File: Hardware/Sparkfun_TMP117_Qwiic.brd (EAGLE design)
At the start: 25.4 x 25.4 mm, 53 parts, among them J1 PTH, J2 QWIIC_RA, J3 QWIIC_RA, U1 TMP117

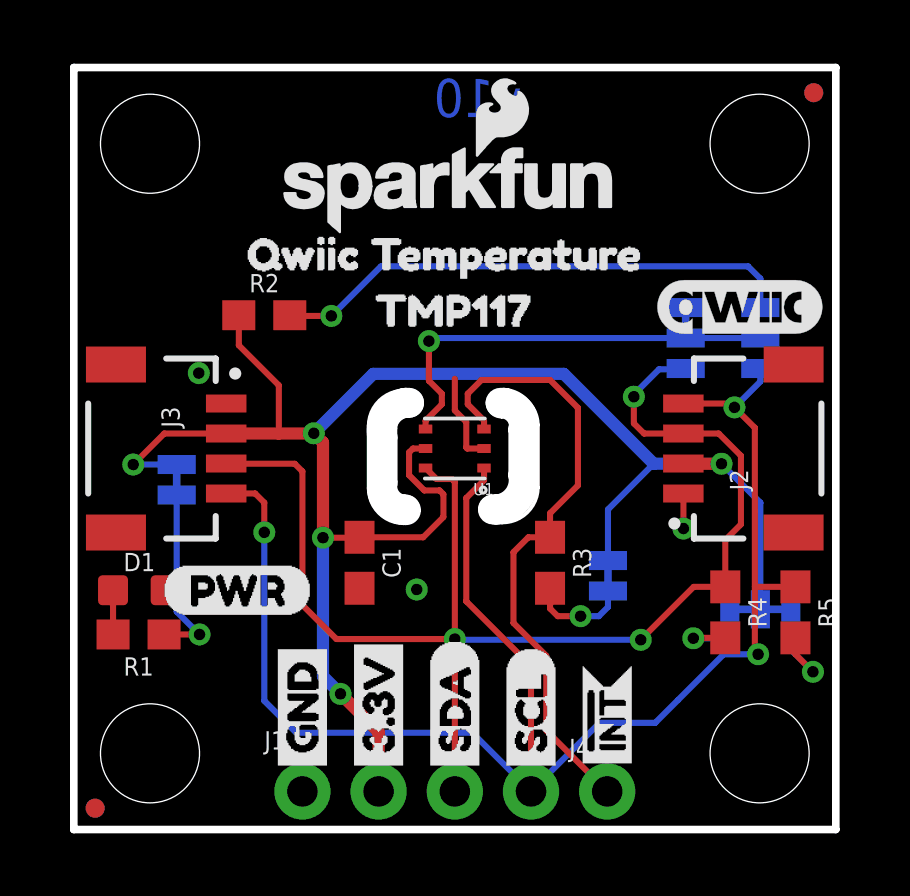
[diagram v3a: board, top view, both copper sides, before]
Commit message: 1st run of checklist
-version font type in schematic
-silk width bumped up to 8 mils on a couple jumpers and the tmp117 package
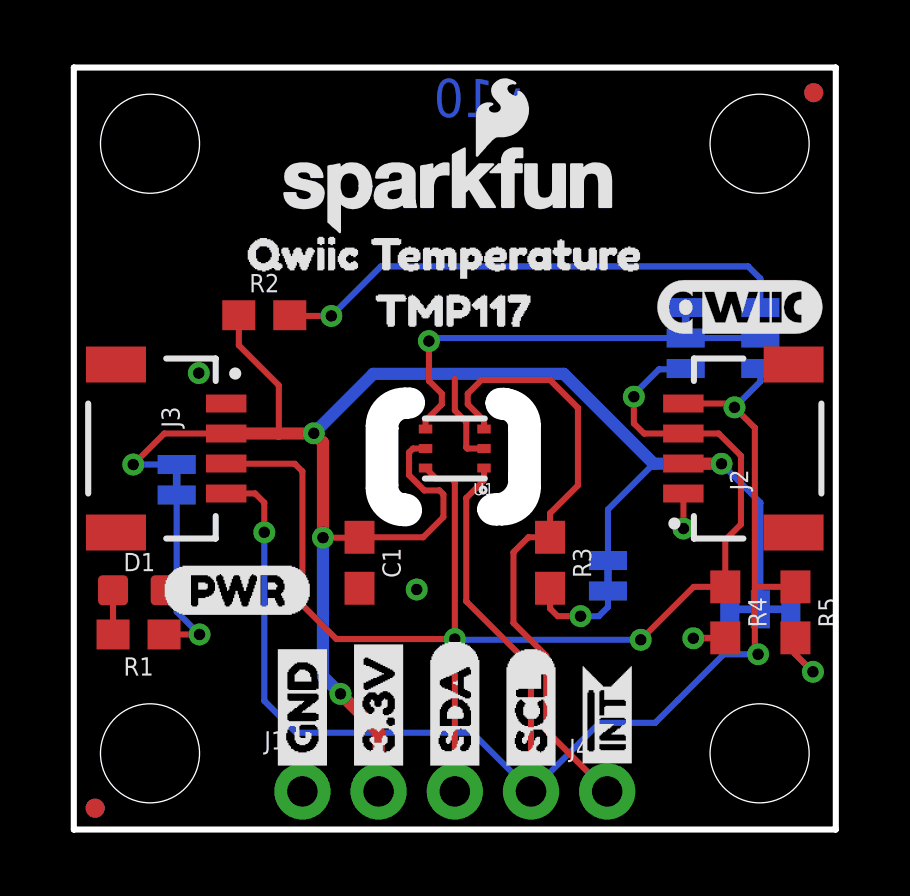
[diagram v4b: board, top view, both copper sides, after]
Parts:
- I2C: value (none) -> JUMPER-SMT_3_2-NC_TRACE_SILK
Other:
- outline, holes or cut-outs redrawn
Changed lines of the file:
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@@
 <setting verticaltext="up"/>
 </settings>
-<grid distance="0.05" unitdist="inch" unit="inch" style="lines" multiple="1" display="yes" altdistance="0.001" altunitdist="inch" altunit="inch"/>
+<grid distance="0.05" unitdist="inch" unit="inch" style="lines" multiple="1" display="yes" altdistance="0.0001" altunitdist="inch" altunit="inch"/>
 <layers>
 <layer number="1" name="Top" color="4" fill="1" visible="yes" active="yes"/>
@@
 <board>
 <plain>
-<wire x1="0" y1="0" x2="0" y2="25.4" width="0.254" layer="20"/>
-<wire x1="25.4" y1="0" x2="0" y2="0" width="0.254" layer="20"/>
-<wire x1="25.4" y1="25.4" x2="25.4" y2="0" width="0.254" layer="20"/>
-<wire x1="0" y1="25.4" x2="25.4" y2="25.4" width="0.254" layer="20"/>
+<wire x1="0" y1="0" x2="0" y2="25.4" width="0.2032" layer="20"/>
+<wire x1="25.4" y1="0" x2="0" y2="0" width="0.2032" layer="20"/>
+<wire x1="25.4" y1="25.4" x2="25.4" y2="0" width="0.2032" layer="20"/>
+<wire x1="0" y1="25.4" x2="25.4" y2="25.4" width="0.2032" layer="20"/>
 <text x="19.431" y="-7.366" size="1.778" layer="51" font="vector" ratio="12" align="top-left">Madison Chodikov,
 Pete Lewis</text>
@@
 <wire x1="11.049" y1="14.224" x2="11.176" y2="14.224" width="1" layer="46"/>
 <wire x1="10.922" y1="10.668" x2="11.049" y2="10.668" width="1" layer="46"/>
-<wire x1="10.7188" y1="13.3604" x2="10.7188" y2="11.4808" width="0.127" layer="20"/>
-<wire x1="10.7188" y1="11.4808" x2="11.0236" y2="11.0998" width="0.127" layer="20" curve="90"/>
-<wire x1="11.0236" y1="11.0998" x2="11.049" y2="11.0998" width="0.127" layer="20"/>
-<wire x1="11.049" y1="11.0998" x2="11.5062" y2="10.6426" width="0.127" layer="20" curve="-90"/>
-<wire x1="11.5062" y1="10.6426" x2="11.0744" y2="10.2108" width="0.127" layer="20" curve="-90"/>
-<wire x1="11.0744" y1="10.2108" x2="10.9982" y2="10.2108" width="0.127" layer="20"/>
-<wire x1="10.9982" y1="10.2108" x2="9.8298" y2="11.3792" width="0.127" layer="20" curve="-90"/>
-<wire x1="9.8298" y1="11.3792" x2="9.8298" y2="13.462" width="0.127" layer="20"/>
-<wire x1="9.8298" y1="13.462" x2="11.0236" y2="14.6304" width="0.127" layer="20" curve="-90"/>
-<wire x1="11.0236" y1="14.6304" x2="11.2014" y2="14.6304" width="0.127" layer="20"/>
-<wire x1="11.2014" y1="14.6304" x2="11.6078" y2="14.224" width="0.127" layer="20" curve="-90"/>
-<wire x1="11.6078" y1="14.224" x2="11.176" y2="13.7922" width="0.127" layer="20" curve="-90"/>
-<wire x1="11.176" y1="13.7922" x2="11.1252" y2="13.7922" width="0.127" layer="20"/>
-<wire x1="11.1252" y1="13.7922" x2="10.7188" y2="13.3858" width="0.127" layer="20" curve="90"/>
-<wire x1="10.7188" y1="13.3858" x2="10.7188" y2="13.3604" width="0.127" layer="20" curve="90"/>
-<wire x1="14.5796" y1="11.684" x2="14.5796" y2="13.3858" width="0.127" layer="20"/>
-<wire x1="14.5796" y1="13.3858" x2="14.2748" y2="13.7668" width="0.127" layer="20" curve="90"/>
-<wire x1="14.2748" y1="13.7668" x2="14.2494" y2="13.7668" width="0.127" layer="20"/>
-<wire x1="14.2494" y1="13.7668" x2="13.7922" y2="14.224" width="0.127" layer="20" curve="-90"/>
-<wire x1="13.7922" y1="14.224" x2="14.224" y2="14.605" width="0.127" layer="20" curve="-90"/>
-<wire x1="14.224" y1="14.605" x2="14.3002" y2="14.605" width="0.127" layer="20"/>
-<wire x1="14.3002" y1="14.605" x2="15.4686" y2="13.4874" width="0.127" layer="20" curve="-90"/>
-<wire x1="15.4686" y1="13.4874" x2="15.4686" y2="11.4046" width="0.127" layer="20"/>
-<wire x1="15.4686" y1="11.4046" x2="14.2748" y2="10.2362" width="0.127" layer="20" curve="-90"/>
-<wire x1="14.2748" y1="10.2362" x2="14.097" y2="10.2362" width="0.127" layer="20"/>
-<wire x1="14.097" y1="10.2362" x2="13.5382" y2="10.668" width="0.127" layer="20" curve="-90"/>
-<wire x1="13.5382" y1="10.668" x2="14.0208" y2="11.0998" width="0.127" layer="20" curve="-90"/>
-<wire x1="14.0208" y1="11.0998" x2="14.097" y2="11.0998" width="0.127" layer="20"/>
-<wire x1="14.097" y1="11.0998" x2="14.5796" y2="11.684" width="0.127" layer="20" curve="90"/>
+<wire x1="10.7188" y1="13.3604" x2="10.7188" y2="11.4808" width="0.2032" layer="20"/>
+<wire x1="10.7188" y1="11.4808" x2="11.0236" y2="11.0998" width="0.2032" layer="20" curve="90"/>
+<wire x1="11.0236" y1="11.0998" x2="11.049" y2="11.0998" width="0.2032" layer="20"/>
+<wire x1="11.049" y1="11.0998" x2="11.5062" y2="10.6426" width="0.2032" layer="20" curve="-90"/>
+<wire x1="11.5062" y1="10.6426" x2="11.0744" y2="10.2108" width="0.2032" layer="20" curve="-90"/>
+<wire x1="11.0744" y1="10.2108" x2="10.9982" y2="10.2108" width="0.2032" layer="20"/>
+<wire x1="10.9982" y1="10.2108" x2="9.8298" y2="11.3792" width="0.2032" layer="20" curve="-90"/>
+<wire x1="9.8298" y1="11.3792" x2="9.8298" y2="13.462" width="0.2032" layer="20"/>
+<wire x1="9.8298" y1="13.462" x2="11.0236" y2="14.6304" width="0.2032" layer="20" curve="-90"/>
+<wire x1="11.0236" y1="14.6304" x2="11.2014" y2="14.6304" width="0.2032" layer="20"/>
+<wire x1="11.2014" y1="14.6304" x2="11.6078" y2="14.224" width="0.2032" layer="20" curve="-90"/>
+<wire x1="11.6078" y1="14.224" x2="11.14551875" y2="13.79981875" width="0.2032" layer="20" curve="-90"/>
+<wire x1="11.14551875" y1="13.79981875" x2="11.09471875" y2="13.79981875" width="0.2032" layer="20"/>
+<wire x1="11.09471875" y1="13.79981875" x2="10.7188" y2="13.3858" width="0.2032" layer="20" curve="90"/>
+<wire x1="10.7188" y1="13.3858" x2="10.7188" y2="13.3604" width="0.2032" layer="20" curve="90"/>
+<wire x1="14.5796" y1="11.684" x2="14.5796" y2="13.3858" width="0.2032" layer="20"/>
+<wire x1="14.5796" y1="13.3858" x2="14.2748" y2="13.7668" width="0.2032" layer="20" curve="90"/>
+<wire x1="14.2748" y1="13.7668" x2="14.297659375" y2="13.75918125" width="0.2032" layer="20"/>
+<wire x1="14.297659375" y1="13.75918125" x2="13.822678125" y2="14.218921875" width="0.2032" layer="20" curve="-90"/>
+<wire x1="13.822678125" y1="14.218921875" x2="14.224" y2="14.599921875" width="0.2032" layer="20" curve="-90"/>
+<wire x1="14.224" y1="14.599921875" x2="14.3002" y2="14.605" width="0.2032" layer="20"/>
+<wire x1="14.3002" y1="14.605" x2="15.4686" y2="13.4874" width="0.2032" layer="20" curve="-90"/>
+<wire x1="15.4686" y1="13.4874" x2="15.4686" y2="11.4046" width="0.2032" layer="20"/>
+<wire x1="15.4686" y1="11.4046" x2="14.2748" y2="10.2362" width="0.2032" layer="20" curve="-90"/>
+<wire x1="14.2748" y1="10.2362" x2="14.097" y2="10.2362" width="0.2032" layer="20"/>
+<wire x1="14.097" y1="10.2362" x2="13.5382" y2="10.668" width="0.2032" layer="20" curve="-90"/>
+<wire x1="13.5382" y1="10.668" x2="14.0208" y2="11.0998" width="0.2032" layer="20" curve="-90"/>
+<wire x1="14.0208" y1="11.0998" x2="14.097" y2="11.0998" width="0.2032" layer="20"/>
+<wire x1="14.097" y1="11.0998" x2="14.5796" y2="11.684" width="0.2032" layer="20" curve="90"/>
 <text x="10.4902" y="11.049" size="0.3048" layer="20" rot="R90">ROUTE OUT</text>
 <text x="15.1384" y="11.1506" size="0.3048" layer="20" rot="R90">ROUTE OUT</text>
@@
 <element name="U$4" library="buzzard_labels" package="TMP1171" value="" x="9.144" y="17.2974" smashed="yes"/>
 <element name="U$6" library="buzzard_labels (2)" package="QWIIC_TEMPERATURE2" value="" x="4.8768" y="19.177" smashed="yes"/>
-<element name="I2C" library="SparkFun-Jumpers" library_urn="urn:adsk.eagle:library:528" package="SMT-JUMPER_3_2-NC_TRACE_SILK" package3d_urn="urn:adsk.eagle:package:39289/1" value="" x="22.8854" y="7.3406" smashed="yes" rot="MR0">
+<element name="I2C" library="SparkFun-Jumpers" package="SMT-JUMPER_3_2-NC_TRACE_SILK" package3d_urn="urn:adsk.eagle:package:39289/1" value="JUMPER-SMT_3_2-NC_TRACE_SILK" x="22.8854" y="7.3406" smashed="yes" rot="MR0">
 <attribute name="NAME" x="22.8854" y="8.4836" size="0.6096" layer="26" font="vector" ratio="20" rot="MR0" align="bottom-center"/>
 <attribute name="VALUE" x="22.8854" y="6.1976" size="0.6096" layer="28" font="vector" ratio="20" rot="MR0" align="top-center"/>
 </element>
-<element name="JP10" library="SparkFun-Jumpers" package="SMT-JUMPER_2_NC_TRACE_SILK" value="INT" x="17.8054" y="8.4582" smashed="yes" rot="MR90">
+<element name="JP10" library="SparkFun-Jumpers" package="SMT-JUMPER_2_NC_TRACE_SILK" package3d_urn="urn:adsk.eagle:package:39281/1" value="INT" x="17.8054" y="8.4582" smashed="yes" rot="MR90">
 <attribute name="NAME" x="19.0754" y="7.5057" size="0.4064" layer="26" rot="MR90"/>
 <attribute name="VALUE" x="16.1544" y="7.5057" size="0.4064" layer="28" rot="MR90"/>
@@
 <attribute name="VALUE" x="24.0284" y="16.383" size="0.6096" layer="28" font="vector" ratio="20" rot="MR270" align="top-center"/>
 </element>
-<element name="JP1" library="SparkFun-Jumpers" library_urn="urn:adsk.eagle:library:528" package="SMT-JUMPER_2_NC_TRACE_SILK" package3d_urn="urn:adsk.eagle:package:39281/1" value="LED" x="3.429" y="11.6586" smashed="yes" rot="MR90">
+<element name="JP1" library="SparkFun-Jumpers" package="SMT-JUMPER_2_NC_TRACE_SILK" package3d_urn="urn:adsk.eagle:package:39281/1" value="LED" x="3.429" y="11.6586" smashed="yes" rot="MR90">
 <attribute name="NAME" x="4.572" y="11.6586" size="0.6096" layer="26" font="vector" ratio="20" rot="MR90" align="bottom-center"/>
 <attribute name="VALUE" x="2.286" y="11.6586" size="0.6096" layer="28" font="vector" ratio="20" rot="MR90" align="top-center"/>

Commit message: checklist catches
-remove package value on jumpers (SCH)
-added VCC range text obj
-fixed drc errors cause by unconnected dimension wires on special route out stuff near IC
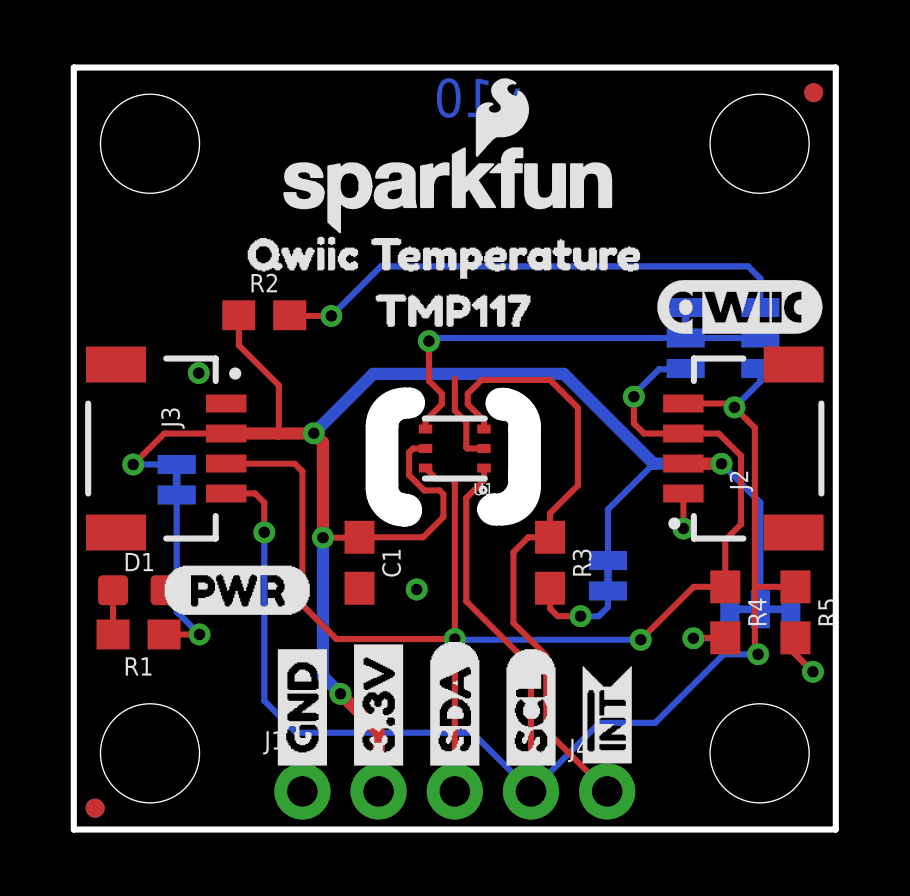
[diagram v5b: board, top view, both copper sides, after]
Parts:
- I2C: value JUMPER-SMT_3_2-NC_TRACE_SILK -> (none)
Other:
- outline, holes or cut-outs redrawn
- board text added: "Madison Chodikov"
- board text added: "Revised by: Pete Lewis"
- board text removed: "Madison Chodikov, Pete Lewis"
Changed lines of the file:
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@@
 <layer number="45" name="Holes" color="7" fill="1" visible="yes" active="yes"/>
 <layer number="46" name="Milling" color="3" fill="1" visible="no" active="yes"/>
-<layer number="47" name="Measures" color="7" fill="1" visible="no" active="yes"/>
+<layer number="47" name="Measures" color="7" fill="1" visible="yes" active="yes"/>
 <layer number="48" name="Document" color="7" fill="1" visible="no" active="yes"/>
 <layer number="49" name="Reference" color="7" fill="1" visible="yes" active="yes"/>
@@
 <wire x1="25.4" y1="25.4" x2="25.4" y2="0" width="0.2032" layer="20"/>
 <wire x1="0" y1="25.4" x2="25.4" y2="25.4" width="0.2032" layer="20"/>
-<text x="19.431" y="-7.366" size="1.778" layer="51" font="vector" ratio="12" align="top-left">Madison Chodikov,
-Pete Lewis</text>
+<text x="19.431" y="-7.366" size="1.778" layer="51" font="vector" ratio="12" align="top-left">Madison Chodikov</text>
 <wire x1="14.986" y1="11.811" x2="14.986" y2="13.335" width="1" layer="46"/>
 <wire x1="14.097" y1="10.668" x2="14.986" y2="11.811" width="1" layer="46" curve="94.763642"/>
@@
 <wire x1="11.049" y1="14.224" x2="11.176" y2="14.224" width="1" layer="46"/>
 <wire x1="10.922" y1="10.668" x2="11.049" y2="10.668" width="1" layer="46"/>
-<wire x1="10.7188" y1="13.3604" x2="10.7188" y2="11.4808" width="0.2032" layer="20"/>
-<wire x1="10.7188" y1="11.4808" x2="11.0236" y2="11.0998" width="0.2032" layer="20" curve="90"/>
-<wire x1="11.0236" y1="11.0998" x2="11.049" y2="11.0998" width="0.2032" layer="20"/>
-<wire x1="11.049" y1="11.0998" x2="11.5062" y2="10.6426" width="0.2032" layer="20" curve="-90"/>
-<wire x1="11.5062" y1="10.6426" x2="11.0744" y2="10.2108" width="0.2032" layer="20" curve="-90"/>
-<wire x1="11.0744" y1="10.2108" x2="10.9982" y2="10.2108" width="0.2032" layer="20"/>
-<wire x1="10.9982" y1="10.2108" x2="9.8298" y2="11.3792" width="0.2032" layer="20" curve="-90"/>
+<wire x1="10.7188" y1="13.4366" x2="10.7188" y2="11.4808" width="0.2032" layer="20"/>
+<wire x1="10.7188" y1="11.4808" x2="10.99058125" y2="11.104878125" width="0.2032" layer="20" curve="90"/>
+<wire x1="10.99058125" y1="11.104878125" x2="11.1125" y2="11.087096875" width="0.2032" layer="20"/>
+<wire x1="11.1125" y1="11.087096875" x2="11.5062" y2="10.6426" width="0.2032" layer="20" curve="-90"/>
+<wire x1="11.5062" y1="10.6426" x2="11.092178125" y2="10.203178125" width="0.2032" layer="20" curve="-90"/>
+<wire x1="11.092178125" y1="10.203178125" x2="10.990578125" y2="10.2006375" width="0.2032" layer="20"/>
+<wire x1="10.990578125" y1="10.2006375" x2="9.8298" y2="11.3792" width="0.2032" layer="20" curve="-90"/>
 <wire x1="9.8298" y1="11.3792" x2="9.8298" y2="13.462" width="0.2032" layer="20"/>
 <wire x1="9.8298" y1="13.462" x2="11.0236" y2="14.6304" width="0.2032" layer="20" curve="-90"/>
 <wire x1="11.0236" y1="14.6304" x2="11.2014" y2="14.6304" width="0.2032" layer="20"/>
 <wire x1="11.2014" y1="14.6304" x2="11.6078" y2="14.224" width="0.2032" layer="20" curve="-90"/>
-<wire x1="11.6078" y1="14.224" x2="11.14551875" y2="13.79981875" width="0.2032" layer="20" curve="-90"/>
-<wire x1="11.14551875" y1="13.79981875" x2="11.09471875" y2="13.79981875" width="0.2032" layer="20"/>
-<wire x1="11.09471875" y1="13.79981875" x2="10.7188" y2="13.3858" width="0.2032" layer="20" curve="90"/>
-<wire x1="10.7188" y1="13.3858" x2="10.7188" y2="13.3604" width="0.2032" layer="20" curve="90"/>
-<wire x1="14.5796" y1="11.684" x2="14.5796" y2="13.3858" width="0.2032" layer="20"/>
-<wire x1="14.5796" y1="13.3858" x2="14.2748" y2="13.7668" width="0.2032" layer="20" curve="90"/>
-<wire x1="14.2748" y1="13.7668" x2="14.297659375" y2="13.75918125" width="0.2032" layer="20"/>
-<wire x1="14.297659375" y1="13.75918125" x2="13.822678125" y2="14.218921875" width="0.2032" layer="20" curve="-90"/>
-<wire x1="13.822678125" y1="14.218921875" x2="14.224" y2="14.599921875" width="0.2032" layer="20" curve="-90"/>
-<wire x1="14.224" y1="14.599921875" x2="14.3002" y2="14.605" width="0.2032" layer="20"/>
-<wire x1="14.3002" y1="14.605" x2="15.4686" y2="13.4874" width="0.2032" layer="20" curve="-90"/>
+<wire x1="11.6078" y1="14.224" x2="11.170915625" y2="13.8049" width="0.2032" layer="20" curve="-90"/>
+<wire x1="11.170915625" y1="13.8049" x2="11.061696875" y2="13.79981875" width="0.2032" layer="20"/>
+<wire x1="11.061696875" y1="13.79981875" x2="10.7188" y2="13.4366" width="0.2032" layer="20" curve="90"/>
+<wire x1="14.5796" y1="11.684" x2="14.592296875" y2="13.4493" width="0.2032" layer="20"/>
+<wire x1="14.592296875" y1="13.4493" x2="14.3484625" y2="13.7287" width="0.2032" layer="20" curve="90"/>
+<wire x1="14.3484625" y1="13.7287" x2="13.832840625" y2="14.180821875" width="0.2032" layer="20" curve="-90"/>
+<wire x1="13.832840625" y1="14.180821875" x2="14.224" y2="14.589759375" width="0.2032" layer="20" curve="-90"/>
+<wire x1="14.224" y1="14.589759375" x2="15.4686" y2="13.4874" width="0.2032" layer="20" curve="-90"/>
 <wire x1="15.4686" y1="13.4874" x2="15.4686" y2="11.4046" width="0.2032" layer="20"/>
 <wire x1="15.4686" y1="11.4046" x2="14.2748" y2="10.2362" width="0.2032" layer="20" curve="-90"/>
@@
 <wire x1="14.097" y1="10.2362" x2="13.5382" y2="10.668" width="0.2032" layer="20" curve="-90"/>
 <wire x1="13.5382" y1="10.668" x2="14.0208" y2="11.0998" width="0.2032" layer="20" curve="-90"/>
-<wire x1="14.0208" y1="11.0998" x2="14.097" y2="11.0998" width="0.2032" layer="20"/>
-<wire x1="14.097" y1="11.0998" x2="14.5796" y2="11.684" width="0.2032" layer="20" curve="90"/>
+<wire x1="14.0208" y1="11.0998" x2="14.1351" y2="11.09471875" width="0.2032" layer="20"/>
+<wire x1="14.1351" y1="11.09471875" x2="14.5796" y2="11.684" width="0.2032" layer="20" curve="90"/>
 <text x="10.4902" y="11.049" size="0.3048" layer="20" rot="R90">ROUTE OUT</text>
 <text x="15.1384" y="11.1506" size="0.3048" layer="20" rot="R90">ROUTE OUT</text>
@@
 <wire x1="19.3802" y1="18.0594" x2="23.7744" y2="18.0594" width="0.3048" layer="22"/>
 <rectangle x1="21.209" y1="14.8844" x2="22.098" y2="17.907" layer="22"/>
+<text x="5.08" y="-11.43" size="1.778" layer="51" font="vector">Revised by: Pete Lewis</text>
 </plain>
 <attributes>
@@
 <element name="U$4" library="buzzard_labels" package="TMP1171" value="" x="9.144" y="17.2974" smashed="yes"/>
 <element name="U$6" library="buzzard_labels (2)" package="QWIIC_TEMPERATURE2" value="" x="4.8768" y="19.177" smashed="yes"/>
-<element name="I2C" library="SparkFun-Jumpers" package="SMT-JUMPER_3_2-NC_TRACE_SILK" package3d_urn="urn:adsk.eagle:package:39289/1" value="JUMPER-SMT_3_2-NC_TRACE_SILK" x="22.8854" y="7.3406" smashed="yes" rot="MR0">
+<element name="I2C" library="SparkFun-Jumpers" package="SMT-JUMPER_3_2-NC_TRACE_SILK" package3d_urn="urn:adsk.eagle:package:39289/1" value="" x="22.8854" y="7.3406" smashed="yes" rot="MR0">
 <attribute name="NAME" x="22.8854" y="8.4836" size="0.6096" layer="26" font="vector" ratio="20" rot="MR0" align="bottom-center"/>
 <attribute name="VALUE" x="22.8854" y="6.1976" size="0.6096" layer="28" font="vector" ratio="20" rot="MR0" align="top-center"/>
@@
 </drawing>
 <compatibility>
-<note version="6.3" minversion="6.2.2" severity="warning">
-Since Version 6.2.2 text objects can contain more than one line,
-which will not be processed correctly with this version.
-</note>
 <note version="8.2" severity="warning">
 Since Version 8.2, EAGLE supports online libraries. The ids
